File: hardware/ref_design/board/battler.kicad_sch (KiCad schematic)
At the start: 9 parts

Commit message: Reference design: QD3525 panel, fab outputs, fit check
The $25-35 Displaytech DT035 is replaced by the QD3525, a bare 3.5in IPS
ST7796U panel of the same class at about $5-8 with a published drawing
and pinout (the panel inside LCDwiki's MSP3525 module).

- J3 is now the landing for its 48-contact solder tail (tools/fp_panel.py),
  wired as the maker's module wires it; TE goes to GPIO32.
- Backlight: an AP3156 charge pump drives each of the six parallel LEDs
  through its own current sink, set over one GPIO (BL_SDI). Its symbol
  comes from tools/sym_lib.py (Konnect's create_symbol draws no body).
- case.scad is built around a fixed panel bay, so the board outline,
  buttons and screws stay put; the lid, lens and STLs follow the panel.
- Routing: fan-out vias kept off pads, the AP3156's GND pins stubbed into
  its thermal pad, loose copper trimmed at the end; silk.py re-runnable.
- fab/: gerbers and drill, JLC BOM (40 part numbers) and CPL (91
  placements), STEP, renders, schematic and assembly PDFs.

check_netlist: PASS. ERC: 0 errors. DRC: 0 errors, 0 unconnected,
0 parity issues (2 cosmetic silk warnings at the USB-C). check_fit: PASS.

Co-Authored-By: Claude Opus 5.5 (1M context) <noreply@anthropic.com>
Claude-Session: https://claude.ai/code/session_01KGgEu3CbFtCsvHRQgAFiCN
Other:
- note added: "48-pin solder FPC of the 3.5in IPS panel,"
- note added: "AP3156 backlight driver"
- note removed: "39-pin FPC to the 3.5in IPS panel,"
- note removed: "TPS61160 backlight boost"
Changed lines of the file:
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@@
         (size 1 1)))
 )
-  (text "39-pin FPC to the 3.5in IPS panel,"
-    (at 100.33 105 0)
+  (text "48-pin solder FPC of the 3.5in IPS panel,"
+    (at 102.87 105 0)
     (effects
       (font
         (size 1 1)))
 )
-  (text "TPS61160 backlight boost"
+  (text "AP3156 backlight driver"
     (at 96.52 108.5 0)
     (effects

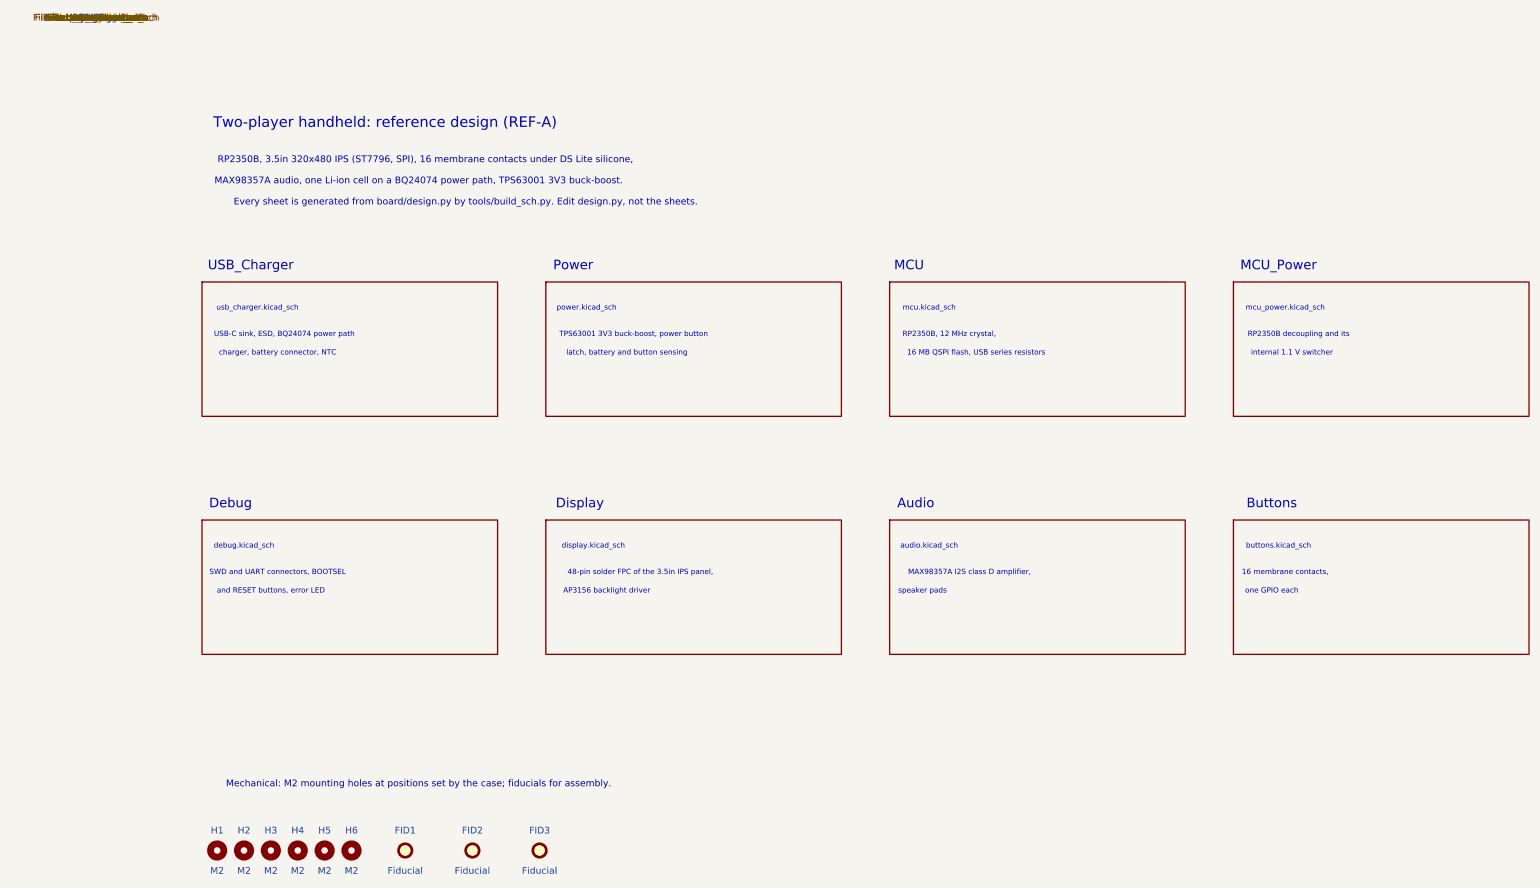
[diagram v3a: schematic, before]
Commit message: 2-layer fork: approved circuit changes in the design data and schematic
TP4056 charger (500 mA, TEMP grounded) with USB load sharing (B5819W, AO3401A
gate fed through a BAT54WS so it switches at once on an unplug, 22 uF on VSYS),
ME6211 3V3 LDO on the power latch, RP2354B with its flash inside (only the
QSPI_SS strap outside), 27 ohm 0603 USB resistors, SRV05-4 ESD, PWM audio
through two RC poles into an FM8002A, seat 1's Y contact as the power button,
no LEDs, no thermistor. Thermal-via footprints use 0.3 mm holes. Netlist
check passes, ERC 0 errors.

Co-Authored-By: Claude Opus 5.5 <noreply@anthropic.com>
Claude-Session: https://claude.ai/code/session_01KGgEu3CbFtCsvHRQgAFiCN
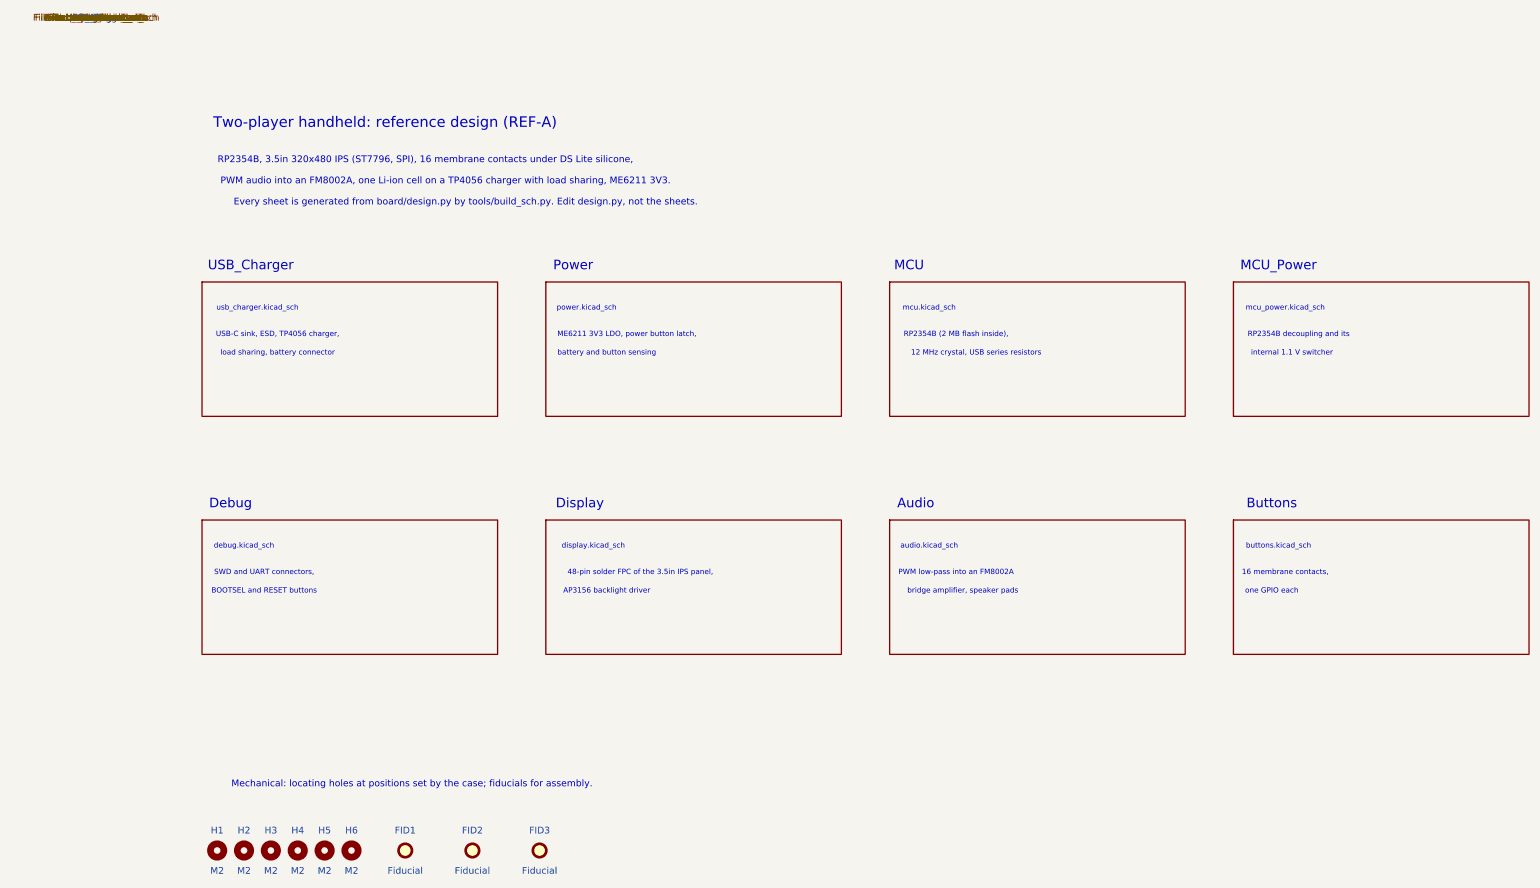
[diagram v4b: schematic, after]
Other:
- note added: "12 MHz crystal, USB series resistors"
- note added: "BOOTSEL and RESET buttons"
- note added: "ME6211 3V3 LDO, power button latch,"
- note added: "Mechanical: locating holes at positions set by the case; fiducials for assembly."
- note added: "PWM audio into an FM8002A, one Li-ion cell on a TP4056 charger with load sharing, ME6211 3V3."
- note added: "PWM low-pass into an FM8002A"
- note added: "RP2354B (2 MB flash inside),"
- note added: "RP2354B decoupling and its"
- note added: "RP2354B, 3.5in 320x480 IPS (ST7796, SPI), 16 membrane contacts under DS Lite silicone,"
- note added: "SWD and UART connectors,"
- note added: "USB-C sink, ESD, TP4056 charger,"
- note added: "battery and button sensing"
- note added: "bridge amplifier, speaker pads"
- note added: "load sharing, battery connector"
- note removed: "16 MB QSPI flash, USB series resistors"
- note removed: "MAX98357A I2S class D amplifier,"
- note removed: "MAX98357A audio, one Li-ion cell on a BQ24074 power path, TPS63001 3V3 buck-boost."
- note removed: "Mechanical: M2 mounting holes at positions set by the case; fiducials for assembly."
- note removed: "RP2350B decoupling and its"
- note removed: "RP2350B, 12 MHz crystal,"
- note removed: "RP2350B, 3.5in 320x480 IPS (ST7796, SPI), 16 membrane contacts under DS Lite silicone,"
- note removed: "SWD and UART connectors, BOOTSEL"
- note removed: "TPS63001 3V3 buck-boost, power button"
- note removed: "USB-C sink, ESD, BQ24074 power path"
- note removed: "and RESET buttons, error LED"
- note removed: "charger, battery connector, NTC"
- note removed: "latch, battery and button sensing"
- note removed: "speaker pads"
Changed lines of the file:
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@@
         (size 2 2)))
 )
-  (text "RP2350B, 3.5in 320x480 IPS (ST7796, SPI), 16 membrane contacts under DS Lite silicone,"
+  (text "RP2354B, 3.5in 320x480 IPS (ST7796, SPI), 16 membrane contacts under DS Lite silicone,"
     (at 62.23 27 0)
     (effects
@@
         (size 1.27 1.27)))
 )
-  (text "MAX98357A audio, one Li-ion cell on a BQ24074 power path, TPS63001 3V3 buck-boost."
-    (at 60.96 31 0)
+  (text "PWM audio into an FM8002A, one Li-ion cell on a TP4056 charger with load sharing, ME6211 3V3."
+    (at 66.04 31 0)
     (effects
       (font
@@
         (size 1.27 1.27)))
 )
-  (text "Mechanical: M2 mounting holes at positions set by the case; fiducials for assembly."
-    (at 60.96 145 0)
+  (text "Mechanical: locating holes at positions set by the case; fiducials for assembly."
+    (at 59.69 145 0)
     (effects
       (font
@@
         (size 1 1)))
 )
-  (text "USB-C sink, ESD, BQ24074 power path"
-    (at 35.56 60 0)
+  (text "USB-C sink, ESD, TP4056 charger,"
+    (at 34.29 60 0)
     (effects
       (font
         (size 1 1)))
 )
-  (text "charger, battery connector, NTC"
+  (text "load sharing, battery connector"
     (at 34.29 63.5 0)
     (effects
@@
         (size 1 1)))
 )
-  (text "TPS63001 3V3 buck-boost, power button"
-    (at 101.6 60 0)
+  (text "ME6211 3V3 LDO, power button latch,"
+    (at 100.33 60 0)
     (effects
       (font
         (size 1 1)))
 )
-  (text "latch, battery and button sensing"
-    (at 100.33 63.5 0)
+  (text "battery and button sensing"
+    (at 96.52 63.5 0)
     (effects
       (font
@@
         (size 1 1)))
 )
-  (text "RP2350B, 12 MHz crystal,"
-    (at 161.29 60 0)
+  (text "RP2354B (2 MB flash inside),"
+    (at 162.56 60 0)
     (effects
       (font
         (size 1 1)))
 )
-  (text "16 MB QSPI flash, USB series resistors"
+  (text "12 MHz crystal, USB series resistors"
     (at 166.37 63.5 0)
     (effects
@@
         (size 1 1)))
 )
-  (text "RP2350B decoupling and its"
+  (text "RP2354B decoupling and its"
     (at 227.33 60 0)
     (effects
@@
         (size 1 1)))
 )
-  (text "SWD and UART connectors, BOOTSEL"
-    (at 34.29 105 0)
+  (text "SWD and UART connectors,"
+    (at 31.75 105 0)
     (effects
       (font
         (size 1 1)))
 )
-  (text "and RESET buttons, error LED"
-    (at 33.02 108.5 0)
+  (text "BOOTSEL and RESET buttons"
+    (at 31.75 108.5 0)
     (effects
       (font
@@
         (size 1 1)))
 )
-  (text "MAX98357A I2S class D amplifier,"
-    (at 165.1 105 0)
+  (text "PWM low-pass into an FM8002A"
+    (at 162.56 105 0)
     (effects
       (font
         (size 1 1)))
 )
-  (text "speaker pads"
-    (at 156.21 108.5 0)
+  (text "bridge amplifier, speaker pads"
+    (at 163.83 108.5 0)
     (effects
       (font

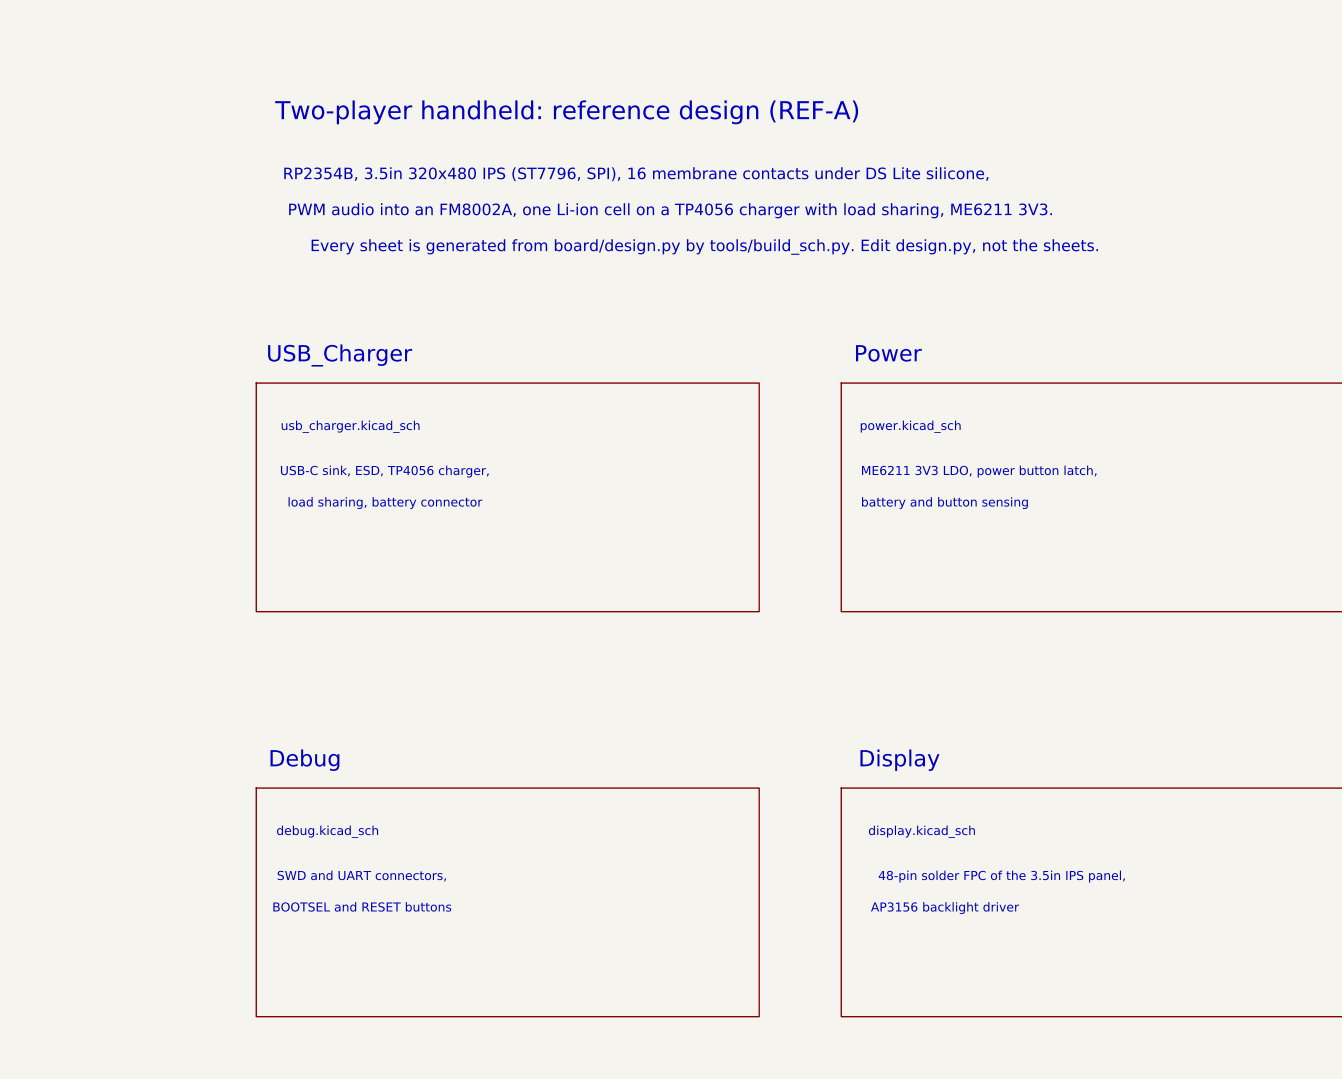
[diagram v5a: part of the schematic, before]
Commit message: Reference design: plug-in ER-TFT035IPS-6 panel, pins and pin escapes for 2 layers
- Panel: EastRising ER-TFT035IPS-6 (ILI9488, 320x480 IPS) on a Hirose FH12-50S
  ZIF connector (J3) that JLC places, instead of the QD3525's hand-soldered tail.
  Case panel/FPC geometry, fit check (FPC zones), backlight sinks paired onto
  its two cathode pins, docs and BOM updated. Prices from both shops' carts:
  about $14.20 a unit at 10 with shipping.
- Pins reassigned for two layers: each faces where its net goes, in fan-out
  order (seat 1's face buttons, panel reset, backlight and ADC inputs on
  GPIO40-47; seat 1's cross and the panel's TE on GPIO28-32).
- build_pcb.copy_escapes: Raspberry Pi's own routing out of the RP2354B's pins,
  copied with the core and locked, so no pin gets boxed in by its neighbours.
  The board now routes completely in about 10 minutes.
- route.py: loose tracks are trimmed back to their last real join instead of
  deleted (Freerouting meets stubs part-way along), T-joins are split and
  duplicate tracks dropped; Freerouting routes to +5 um clearance and a 0.12 mm
  inset outline (it rounded under 0.15 mm and hugged the board edge).
- MCU sheet region widened for the longer labels; datasheet list updated for
  the 2-layer parts; old panel landing footprint/tool and the unused side
  switch footprint removed.

Checks: netlist PASS (122 parts, 115 nets), ERC 0, DRC 0 errors / 0
unconnected / 0 parity (2 cosmetic silk warnings), holes 0.3/0.6/0.65/2.2 mm,
fit PASS on 91 parts.

Co-Authored-By: Claude Opus 5.5 <noreply@anthropic.com>
Claude-Session: https://claude.ai/code/session_01KGgEu3CbFtCsvHRQgAFiCN
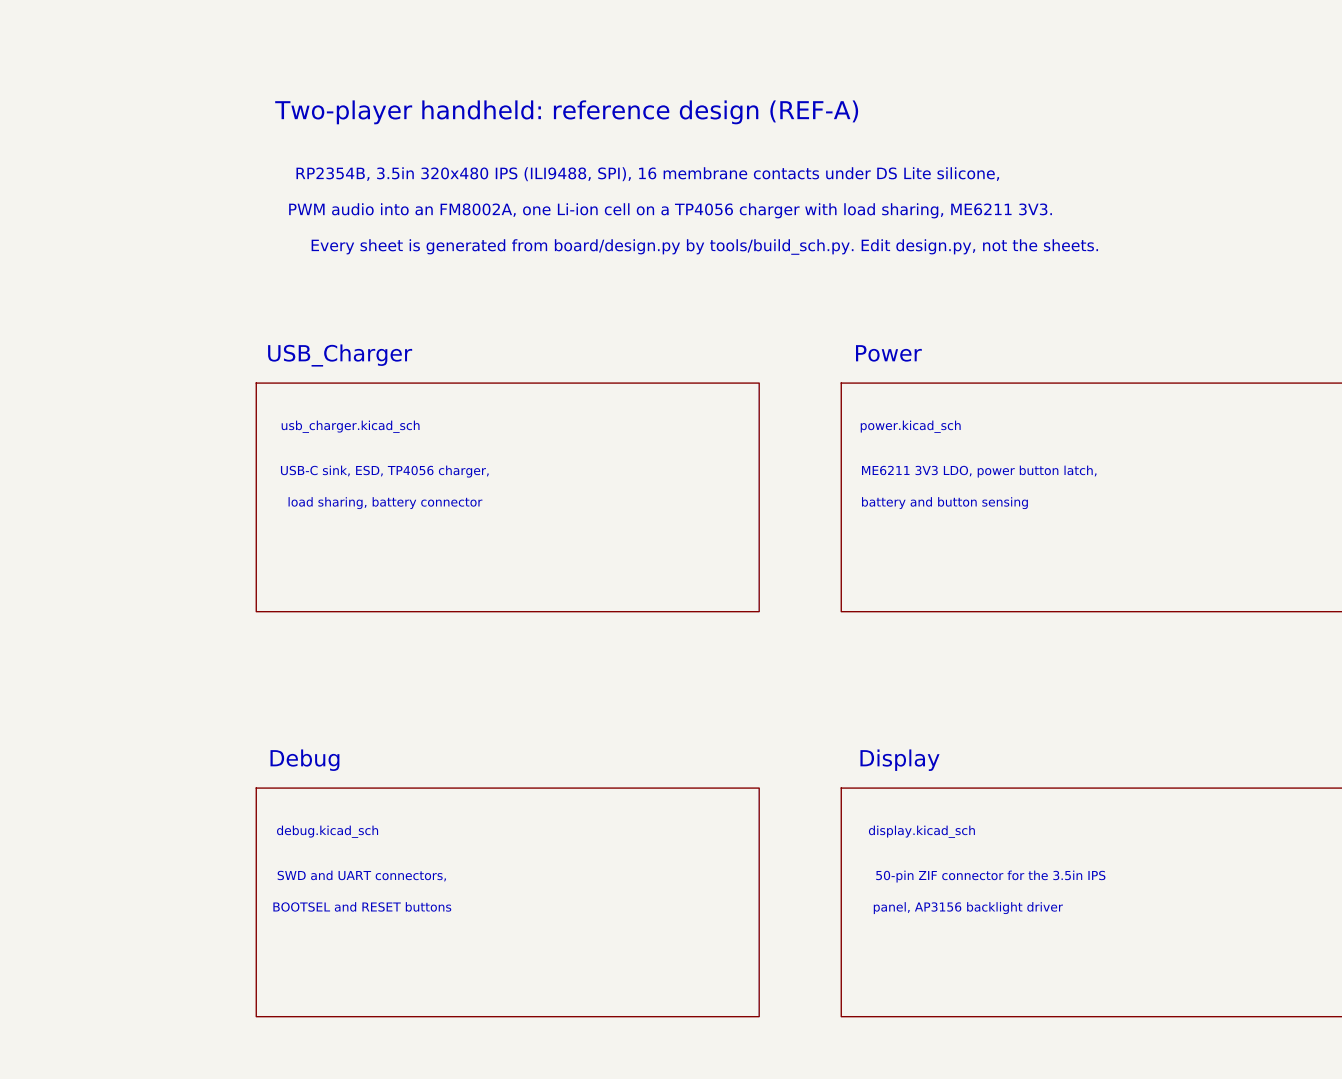
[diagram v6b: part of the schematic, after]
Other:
- note added: "50-pin ZIF connector for the 3.5in IPS"
- note added: "RP2354B, 3.5in 320x480 IPS (ILI9488, SPI), 16 membrane contacts under DS Lite silicone,"
- note added: "panel, AP3156 backlight driver"
- note removed: "48-pin solder FPC of the 3.5in IPS panel,"
- note removed: "AP3156 backlight driver"
- note removed: "RP2354B, 3.5in 320x480 IPS (ST7796, SPI), 16 membrane contacts under DS Lite silicone,"
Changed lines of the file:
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@@
         (size 2 2)))
 )
-  (text "RP2354B, 3.5in 320x480 IPS (ST7796, SPI), 16 membrane contacts under DS Lite silicone,"
-    (at 62.23 27 0)
+  (text "RP2354B, 3.5in 320x480 IPS (ILI9488, SPI), 16 membrane contacts under DS Lite silicone,"
+    (at 63.5 27 0)
     (effects
       (font
@@
         (size 1 1)))
 )
-  (text "48-pin solder FPC of the 3.5in IPS panel,"
-    (at 102.87 105 0)
+  (text "50-pin ZIF connector for the 3.5in IPS"
+    (at 101.6 105 0)
     (effects
       (font
         (size 1 1)))
 )
-  (text "AP3156 backlight driver"
-    (at 96.52 108.5 0)
+  (text "panel, AP3156 backlight driver"
+    (at 99.06 108.5 0)
     (effects
       (font
